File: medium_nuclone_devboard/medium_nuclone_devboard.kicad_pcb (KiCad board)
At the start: 2 copper layers, 48.3 x 76.2 mm, 39 parts, among them J1 JTAG_2X05, J2 TYPE-C-31-M-12, J3 nuclone_medium_left, J4 nuclone_medium_right, SW1 RESET, SW2 Bootloader, U1 MCP1702-MB

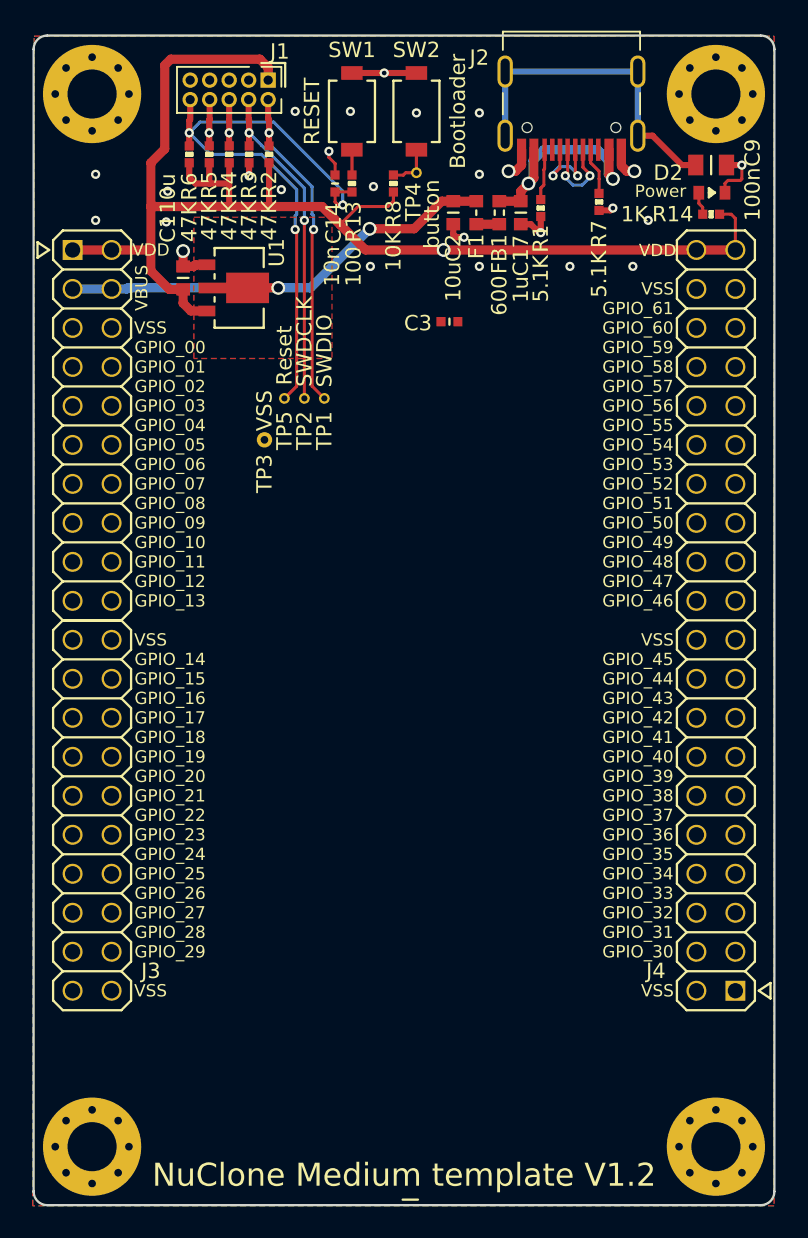
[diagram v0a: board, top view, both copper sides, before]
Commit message: adjusted edges of medium nuclones
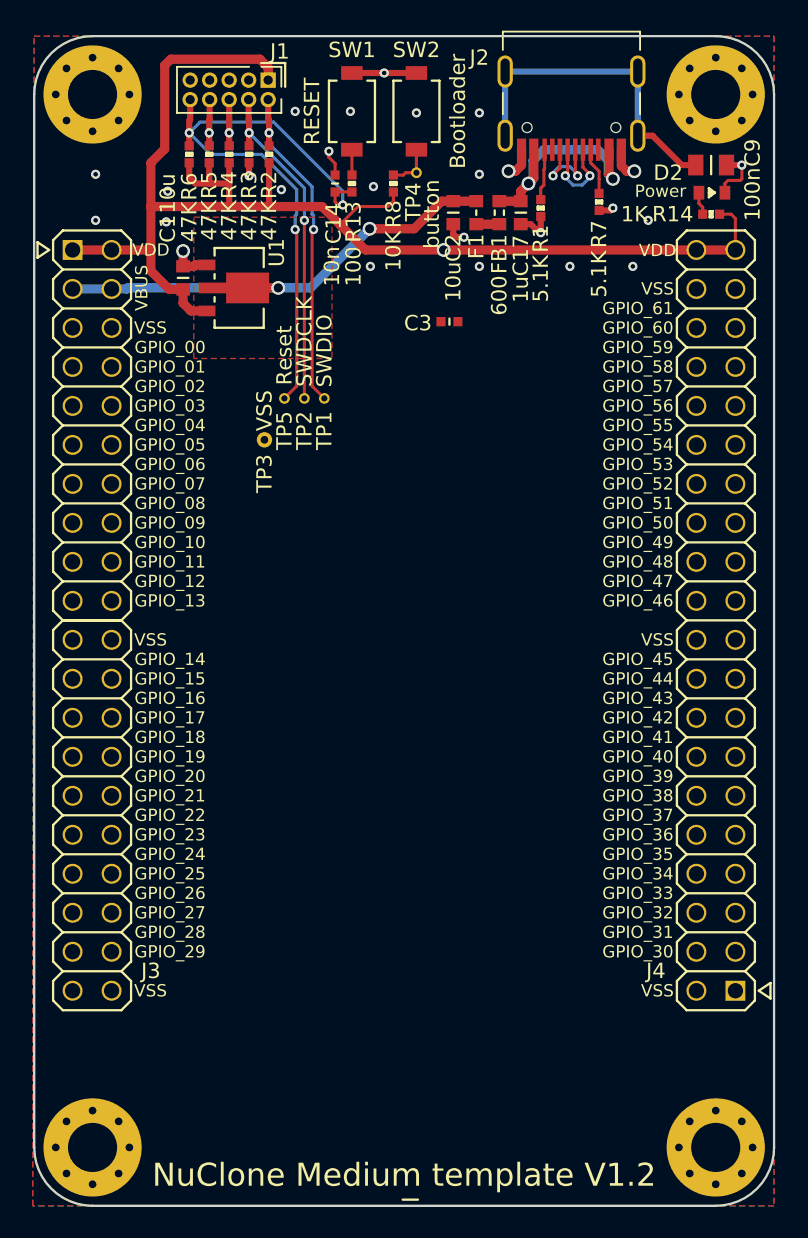
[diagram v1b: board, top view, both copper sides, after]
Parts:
- N2: value 20210829 -> 20210921
- moved H4 0.06 mm to (64.8, 133.4)
- moved H3 0.05 mm to (105.4, 133.4)
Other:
- board size 48.3 x 76.2 mm -> 48.2 x 76.2 mm

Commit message: fixed groundplane medium nuclone, fixed USB-c routing
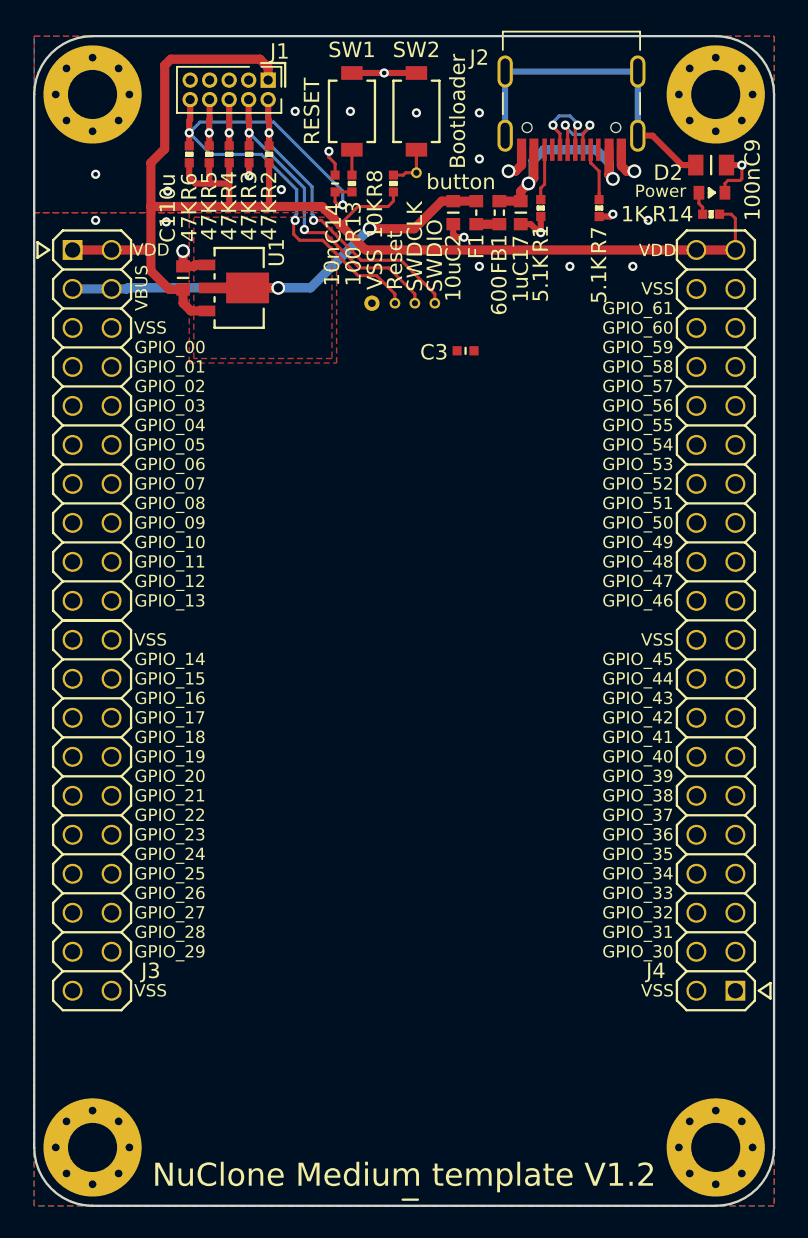
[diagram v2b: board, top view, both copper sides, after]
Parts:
- moved TP3 11.3 mm to (83.0, 78.4)
- moved TP2 9.50 mm to (85.8, 78.4)
- moved TP5 9.50 mm to (84.5, 78.4)
- moved TP1 9.50 mm to (87.1, 78.4)
- moved C3 2.17 mm to (89.1, 81.5)
- moved R7 0.40 mm to (97.8, 72.2)
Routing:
- net /RESET: track 41.0 -> 38.8 mm
- net /TMS: track 21.9 -> 20.4 mm
- net /TCK: track 21.8 -> 20.4 mm
- net /VDD: track 90.2 -> 90.1 mm, vias 1 -> 0
- net /VSS: vias 26 -> 24

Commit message: added nuclone template versionnumber
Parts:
- added N5: Nuclone Template 20211109, SquantorLabels:Label_Generic, B.Cu at (79.6, 62.2)
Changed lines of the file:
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@@
     (tracks 248)
     (zones 0)
-    (modules 39)
+    (modules 40)
     (nets 84)
   )
@@
     (uvia_drill 0.3)
   )
+  (module SquantorLabels:Label_Generic (layer B.Cu)
+    (at 79.629 62.23 180)
+    (descr "Label for general purpose use")
+    (tags Label)
+    (attr smd)
+    (fp_text reference N5 (at 0 -1.85) (layer B.Fab) hide
+      (effects (font (size 1 1) (thickness 0.15)) (justify mirror))
+    )
+    (fp_text value "Nuclone Template 20211109" (at 0.8 0.1) (layer B.SilkS)
+      (effects (font (size 0.8 0.8) (thickness 0.15)) (justify mirror))
+    )
+    (fp_line (start -0.5 -0.6) (end 0.5 -0.6) (layer B.SilkS) (width 0.15))
+  )
   (module SquantorConnectorsNamed:nuclone_medium_left (layer F.Cu)

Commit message: WIP modifying medium nuclone to have stacked headers
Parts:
- J4: footprint SquantorConnectorsNamed:nuclone_medium_right -> SquantorConnectorsNamed:nuclone_medium_right_stacked

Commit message: updated medium nuclone template
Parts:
- J3: footprint SquantorConnectorsNamed:nuclone_medium_left -> SquantorConnectorsNamed:nuclone_medium_left_stacked
- N2: value 20210921 -> 20211121
- N5: value Nuclone Template 20211109 -> Nuclone Template 20211121
- moved C1 2.50 mm to (73.2, 76.8)
- moved U1 2.50 mm to (76.5, 77.5)
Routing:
- net /VBUS: track 32.4 -> 35.2 mm
- net /VDD: track 90.1 -> 91.2 mm
- net Net-(C17-Pad2): track 15.5 -> 16.4 mm
- net /VSS: vias 24 -> 23

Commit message: small routing improvements
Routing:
- net /RESET: track 38.8 -> 28.4 mm

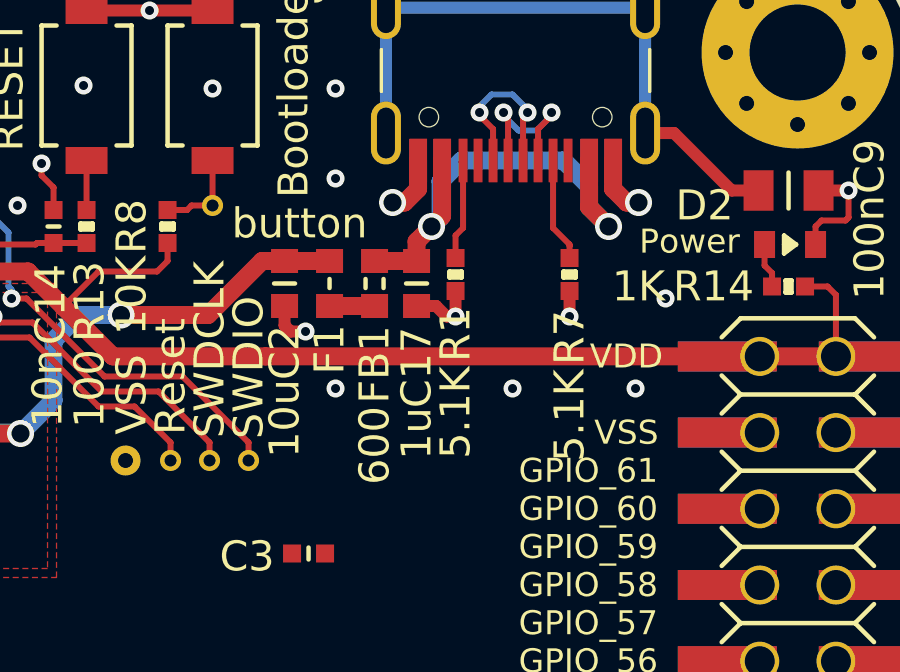
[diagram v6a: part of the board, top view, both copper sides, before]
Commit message: updated nuclone templates
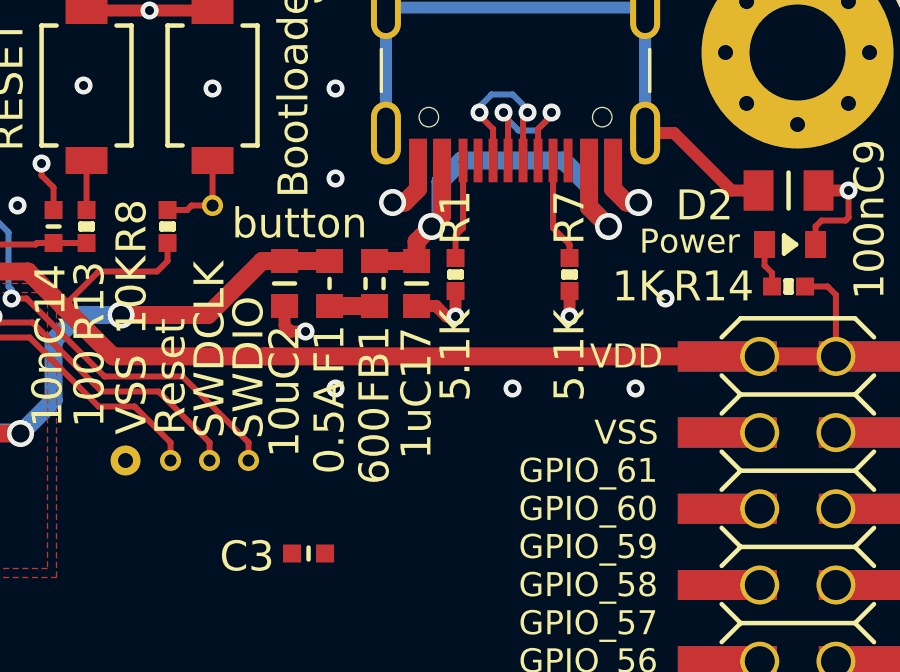
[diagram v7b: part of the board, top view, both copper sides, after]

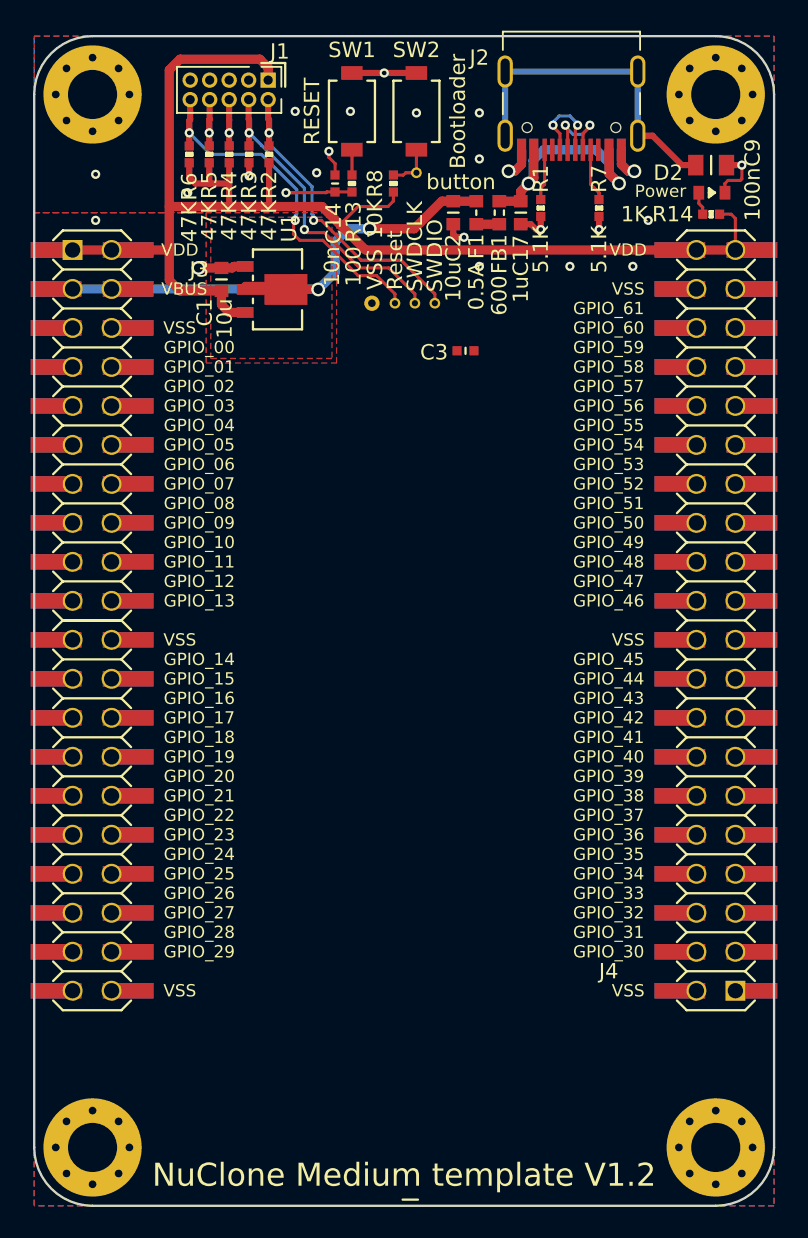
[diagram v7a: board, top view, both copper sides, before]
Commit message: conversion to kicad 7
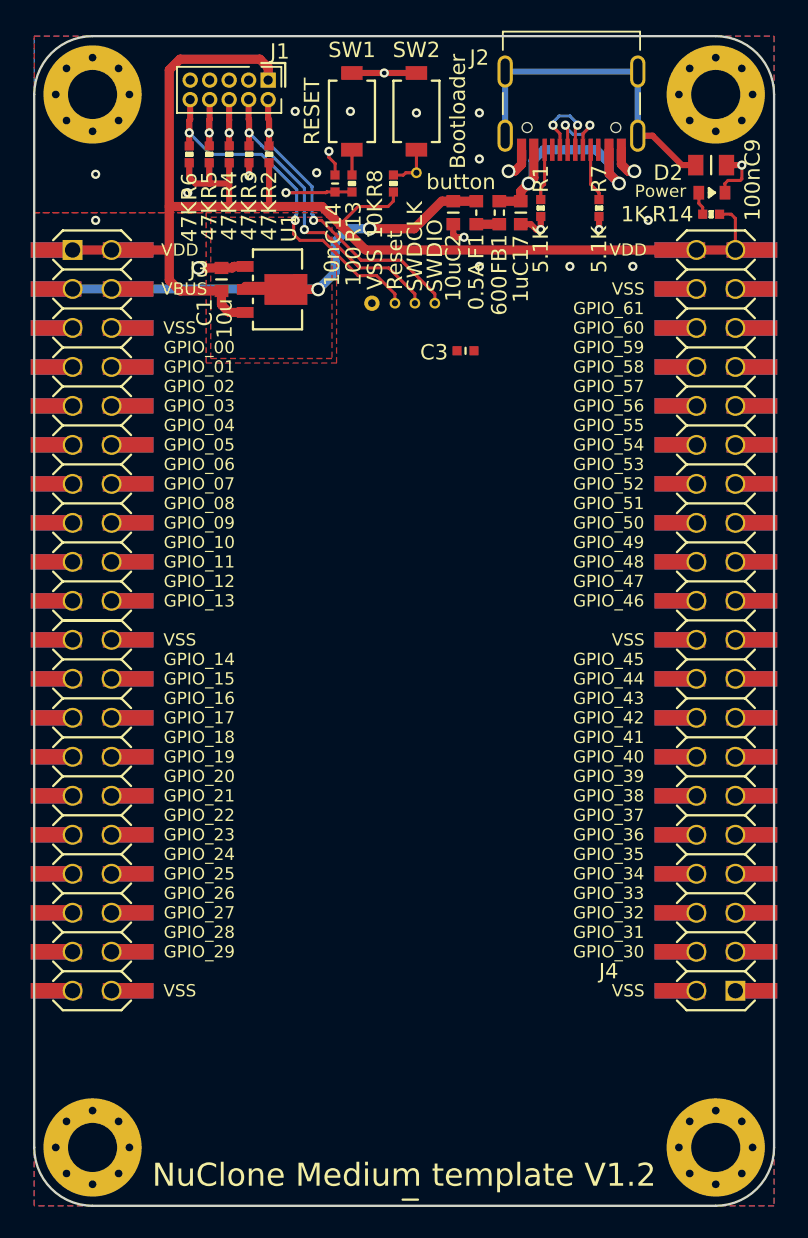
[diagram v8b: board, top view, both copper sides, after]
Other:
- net class Default removed
- net class Power removed
- net class Signal removed
